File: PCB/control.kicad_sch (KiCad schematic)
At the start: 0 parts

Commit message: Cleaned up the schematic and got started on assigning all the footprints to the symbols
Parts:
- added C20, C21: 0.1 µF, Capacitor_THT:C_Radial_D5.0mm_H5.0mm_P2.00mm, symbol Device:C
- added D38, D39, D40, D41, D42, D43, D44, D45, D46, D47, D48, D49, D50, D51, D52, D53: BLUE, LED_THT:LED_D1.8mm_W1.8mm_H2.4mm_Horizontal_O1.27mm_Z1.6mm, symbol Device:LED
- added D54, D55, D56, D57, D58: GREEN, LED_THT:LED_D1.8mm_W1.8mm_H2.4mm_Horizontal_O1.27mm_Z1.6mm, symbol Device:LED
- added D59, D60, D61: RED, LED_THT:LED_D1.8mm_W1.8mm_H2.4mm_Horizontal_O1.27mm_Z1.6mm, symbol Device:LED
- added R40, R41, R42, R43, R44, R45, R46, R47, R48, R49, R50, R51, R52, R53, R54, R55, R56, R57, R58, R59, R60, R61, R62, R63: 220, Resistor_THT:R_Axial_DIN0207_L6.3mm_D2.5mm_P7.62mm_Horizontal, symbol Device:R
- added R64: 1k, Resistor_THT:R_Axial_DIN0207_L6.3mm_D2.5mm_P7.62mm_Horizontal, symbol Device:R
- added SW8: SW_Push, Button_Switch_THT:SW_PUSH_6mm, symbol Switch:SW_Push
- added U26, U45: 74LS00, symbol 74xx:74LS00
- added U27, U28, U46, U47: 74LS04, symbol 74xx:74LS04
- added U41: 74LS161, symbol 74xx:74LS161
- added U42: 74LS138, symbol 74xx:74LS138
- added U43, U44: AT28C64B-15PU, AT28C64B_15PU:DIP1555W45P254L3733H482Q28, symbol AT28C64B-15PU:AT28C64B-15PU
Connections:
- new net: D44.2 (A), U28.11, U43.12 (I/O1)
- new net: D54.1 (K), U42.11 (O4)
- new net: D54.2 (A), R60.1
- new net: D57.1 (K), U42.14 (O1)
- new net: D57.2 (A), R57.1
- new net: D51.1 (K), R53.1
- new net: D51.2 (A), U44.13 (I/O2), U46.13
- new net: D49.1 (K), R51.1
- new net: R64.1, SW8.1, U26.10, U26.9
- new net: D41.1 (K), R43.1
- new net: D58.2 (A), R56.1
- new net: D59.2 (A), U41.14 (Q0), U42.1 (A0), U43.10 (A0), U44.10 (A0)
- new net: D53.2 (A), U44.11 (I/O0), U46.5
- new net: D52.2 (A), U44.12 (I/O1), U46.11
- new net: D48.2 (A), U44.17 (I/O5), U47.3
- new net: D46.2 (A), U44.19 (I/O7), U47.1
- new net: D61.2 (A), U41.12 (Q2), U42.3 (A2), U43.8 (A2), U44.8 (A2)
- new net: D60.2 (A), U41.13 (Q1), U42.2 (A1), U43.9 (A1), U44.9 (A1)
- new net: D45.2 (A), U28.9, U43.11 (I/O0)
- new net: D52.1 (K), R54.1
- new net: D61.1 (K), R63.1
- new net: D60.1 (K), R62.1
- new net: U26.5, U42.10 (O5)
- new net: U26.6, U45.1, U45.2
- new net: D40.1 (K), R42.1
- new net: D55.1 (K), U42.12 (O3)
- new net: D55.2 (A), R59.1
- new net: D58.1 (K), U42.15 (O0)
- new net: D56.1 (K), U42.13 (O2)
- new net: D56.2 (A), R58.1
- new net: D43.2 (A), U28.13, U43.13 (I/O2)
- new net: D42.2 (A), U28.5, U43.15 (I/O3)
- new net: D41.2 (A), U43.16 (I/O4), U46.3
- new net: D39.2 (A), U43.18 (I/O6), U46.1
- new net: D39.1 (K), R41.1
- new net: D47.1 (K), R49.1
- new net: U41.1 (~{MR}), U45.3
- new net: D53.1 (K), R55.1
- new net: D48.1 (K), R50.1
- new net: D42.1 (K), R44.1
- new net: D45.1 (K), R47.1
- new net: D59.1 (K), R61.1
- new net: D43.1 (K), R45.1
- new net: D46.1 (K), R48.1
- new net: D44.1 (K), R46.1
- new net: D50.1 (K), R52.1
- new net: D38.1 (K), R40.1
- new net CE: D50.2 (A), U44.15 (I/O3)
- new net CF: U43.25 (A8), U44.25 (A8)
- new net CLR: U26.11
- new net GND: C20.2, C21.2, R61.2, R62.2, R63.2, R64.2, U27.7 (GND), U42.4 (E1), U42.5 (E2), U43.14 (GND), U43.2 (A12), U43.20 (~{CE}), U43.21 (A10), U43.22 (~{OE}), U43.23 (A11), U43.3 (A7), U44.14 (GND), U44.2 (A12), U44.20 (~{CE}), U44.21 (A10), U44.22 (~{OE}), U44.23 (A11), U45.7 (GND), U46.7 (GND)
- new net HLT: D38.2 (A), U43.19 (I/O7)
- new net IR_4: U43.7 (A3), U44.7 (A3)
- new net IR_5: U43.6 (A4), U44.6 (A4)
- new net IR_6: U43.5 (A5), U44.5 (A5)
- new net IR_7: U43.4 (A6), U44.4 (A6)
- new net OI: D49.2 (A), U44.16 (I/O4)
- new net RI: D40.2 (A), U43.17 (I/O5)
- new net SU: D47.2 (A), U44.18 (I/O6)
- new net VCC: C20.1, C21.1, R56.2, R57.2, R58.2, R59.2, R60.2, SW8.2, U27.14 (VCC), U41.10 (CET), U41.7 (CEP), U41.9 (~{PE}), U42.6 (E3), U43.27 (~{WE}), U43.28 (VCC), U44.27 (~{WE}), U44.28 (VCC), U44.3 (A7), U45.14 (VCC), U46.14 (VCC)
- new net ZF: U43.24 (A9), U44.24 (A9)
- new net ~{AI}: U28.10
- new net ~{AO}: U28.8
- new net ~{BI}: U47.4
- new net ~{CLK}: U41.2 (CP)
- new net ~{CLR}: U26.12, U26.13, U26.4, U26.8
- new net ~{CO}: U46.12
- new net ~{EO}: U47.2
- new net ~{FI}: U46.6
- new net ~{II}: U28.12
- new net ~{IO}: U28.6
- new net ~{J}: U46.10
- new net ~{MI}: U46.2
- new net ~{RO}: U46.4
- no-connect marks 0 -> 10

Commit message: added more models to work with on my pcb
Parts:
- D38, D39, D40, D41, D42, D43, D44, D45, D46, D47, D48, D49, D50, D51, D52, D53, D54, D55, D56, D57, D58, D59, D60, D61: footprint LED_THT:LED_D1.8mm_W1.8mm_H2.4mm_Horizontal_O1.27mm_Z1.6mm -> LED_THT:LED_D3.0mm
- U26, U27, U28, U45, U46, U47: footprint (none) -> Custom:N14
- U41, U42: footprint (none) -> Custom:N16
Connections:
- net GND: now also R40.2, R41.2, R42.2, R43.2, R44.2, R45.2, R46.2, R47.2, R48.2, R49.2, R50.2, R51.2, R52.2, R53.2, R54.2, R55.2

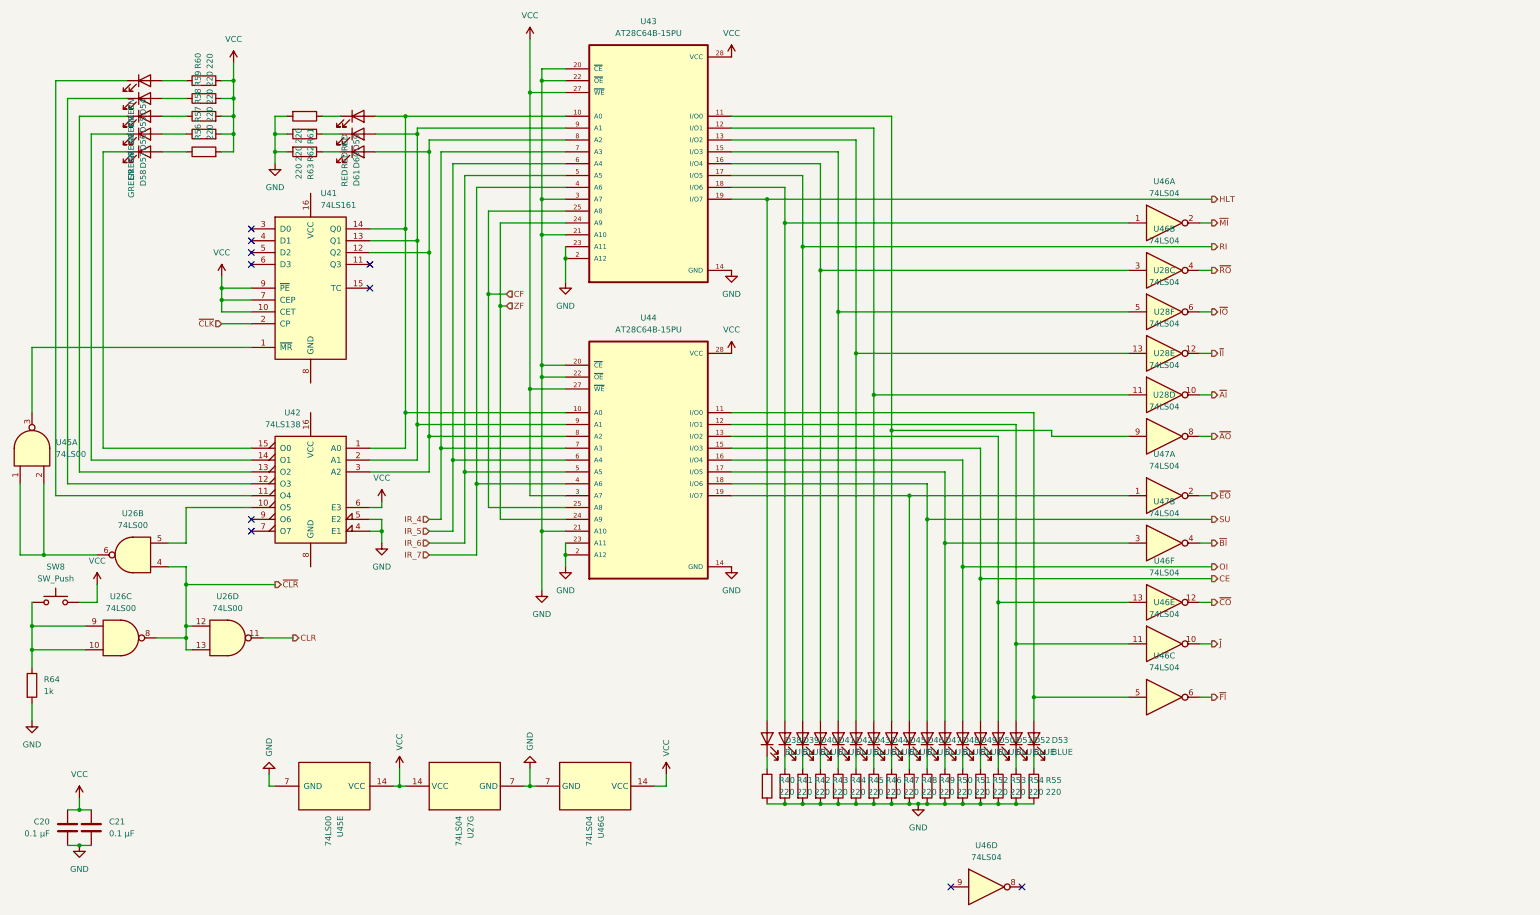
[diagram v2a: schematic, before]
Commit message: Fixed a bunch of ERC errors so know there is only one remaining.
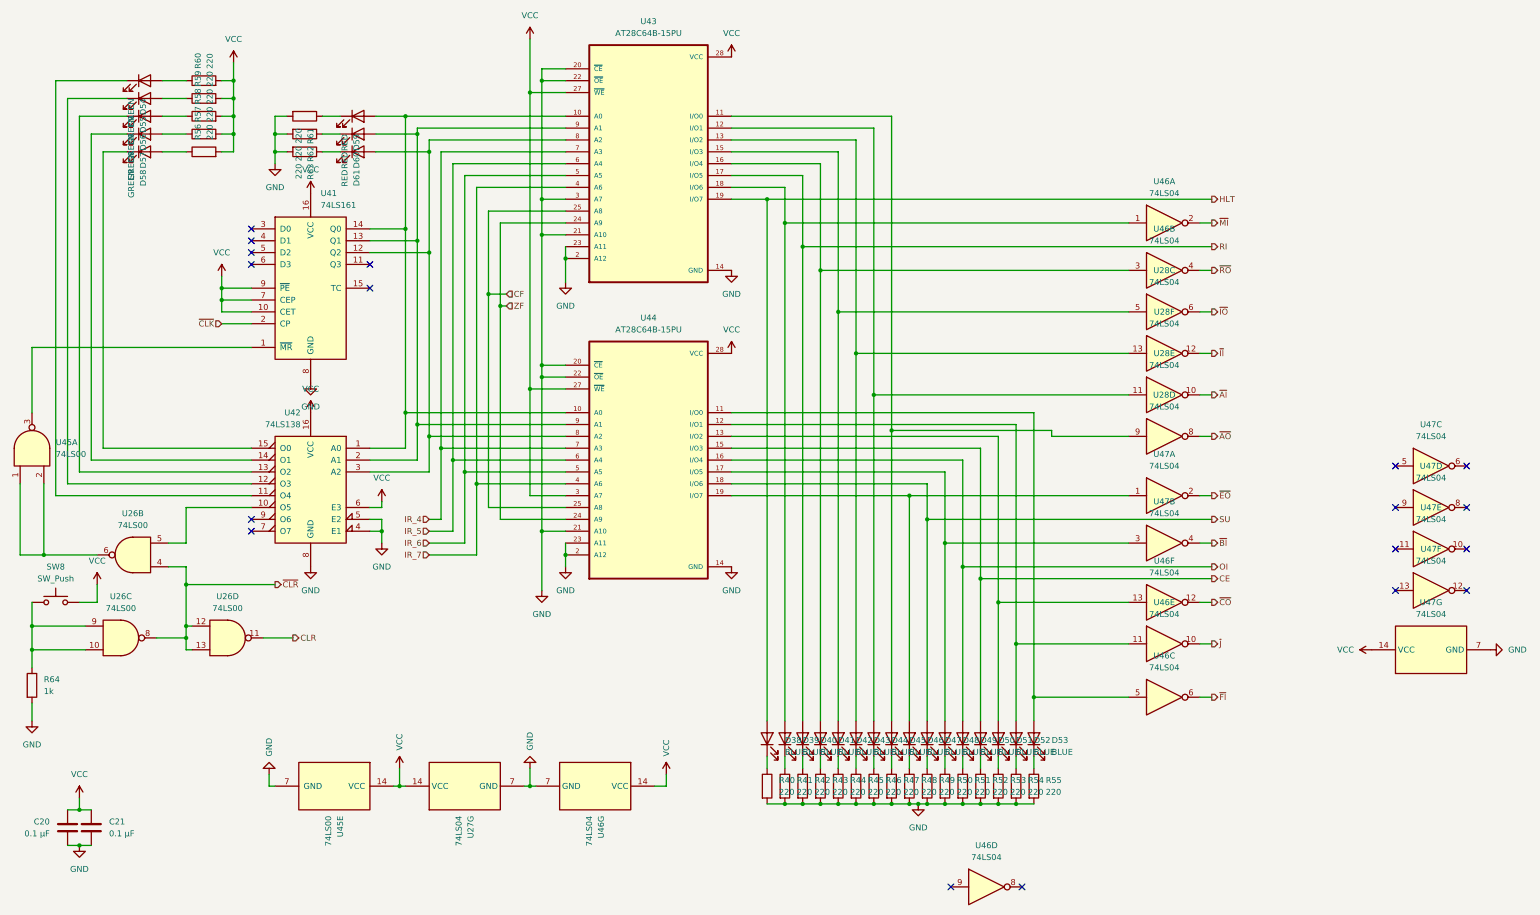
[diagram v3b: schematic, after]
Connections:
- net GND: now also U41.8 (GND), U42.8 (GND), U47.7 (GND)
- net VCC: now also U41.16 (VCC), U42.16 (VCC), U47.14 (VCC)
- no-connect marks 10 -> 18
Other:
- moved on the sheet: U47D

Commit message: Routed the traces for the ground
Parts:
- added unit 3 of U47
- added unit 5 of U47
- added unit 7 of U47
- added unit 6 of U47
- added unit 2 of U47
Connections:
- net GND: now also U47.7 (GND); no longer U47.7 (GND)
- net VCC: now also U47.14 (VCC); no longer U47.14 (VCC)
- net ~{BI}: now also U47.4; no longer U47.4
- net at D48.2 (A), U44.17 (I/O5): now also U47.3; no longer U47.3
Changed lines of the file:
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@@
+	(symbol
+		(lib_id "74xx:74LS04")
+		(at 317.5 147.32 90)
+		(unit 7)
+		(exclude_from_sim no)
+		(in_bom yes)
+		(on_board yes)
+		(dnp no)
+		(fields_autoplaced yes)
+		(property "Reference" "U47"
+			(at 317.5 137.16 90)
+			(effects
+				(font
+					(size 1.27 1.27)
+				)
+			)
+		)
+		(property "Value" "74LS04"
+			(at 317.5 139.7 90)
+			(effects
+				(font
+					(size 1.27 1.27)
+				)
+			)
+		)
+		(property "Footprint" "Custom:N14"
+			(at 317.5 147.32 0)
+			(effects
+				(font
+					(size 1.27 1.27)
+				)
+				(hide yes)
+			)
+		)
+		(property "Datasheet" "http://www.ti.com/lit/gpn/sn74LS04"
+			(at 317.5 147.32 0)
+			(effects
+				(font
+					(size 1.27 1.27)
+				)
+				(hide yes)
+			)
+		)
+		(property "Description" "Hex Inverter"
+			(at 317.5 147.32 0)
+			(effects
+				(font
+					(size 1.27 1.27)
+				)
+				(hide yes)
+			)
+		)
+		(pin "3"
+		)
+		(pin "2"
+		)
+		(pin "1"
+		)
+		(pin "4"
+		)
+		(pin "9"
+		)
+		(pin "6"
+		)
+		(pin "5"
+		)
+		(pin "14"
+		)
+		(pin "12"
+		)
+		(pin "8"
+		)
+		(pin "11"
+		)
+		(pin "13"
+		)
+		(pin "10"
+		)
+		(pin "7"
+		)
+		(instances
+			(project ""
+				(path "/48633dea-2de9-4b6f-aeff-2ee54233f918/d073e50d-b064-481f-8def-abf1072e09eb"
+					(reference "U47")
+					(unit 7)
+				)
+			)
+		)
+	)
 	(symbol
 		(lib_id "74xx:74LS04")
@@
 				)
 			)
-		)
-	)
-	(symbol
-		(lib_id "74xx:74LS04")
-		(at 317.5 147.32 90)
-		(unit 7)
-		(exclude_from_sim no)
-		(in_bom yes)
-		(on_board yes)
-		(dnp no)
-		(fields_autoplaced yes)
-		(property "Reference" "U47"
-			(at 317.5 137.16 90)
-			(effects
-				(font
-					(size 1.27 1.27)
-				)
-			)
-		)
-		(property "Value" "74LS04"
-			(at 317.5 139.7 90)
-			(effects
-				(font
-					(size 1.27 1.27)
-				)
-			)
-		)
-		(property "Footprint" "Custom:N14"
-			(at 317.5 147.32 0)
-			(effects
-				(font
-					(size 1.27 1.27)
-				)
-				(hide yes)
-			)
-		)
-		(property "Datasheet" "http://www.ti.com/lit/gpn/sn74LS04"
-			(at 317.5 147.32 0)
-			(effects
-				(font
-					(size 1.27 1.27)
-				)
-				(hide yes)
-			)
-		)
-		(property "Description" "Hex Inverter"
-			(at 317.5 147.32 0)
-			(effects
-				(font
-					(size 1.27 1.27)
-				)
-				(hide yes)
-			)
-		)
-		(pin "3"
-		)
-		(pin "2"
-		)
-		(pin "1"
-		)
-		(pin "4"
-		)
-		(pin "9"
-		)
-		(pin "6"
-		)
-		(pin "5"
-		)
-		(pin "14"
-		)
-		(pin "12"
-		)
-		(pin "8"
-		)
-		(pin "11"
-		)
-		(pin "13"
-		)
-		(pin "10"
-		)
-		(pin "7"
-		)
-		(instances
-			(project ""
-				(path "/48633dea-2de9-4b6f-aeff-2ee54233f918/d073e50d-b064-481f-8def-abf1072e09eb"
-					(reference "U47")
-					(unit 7)
-				)
-			)

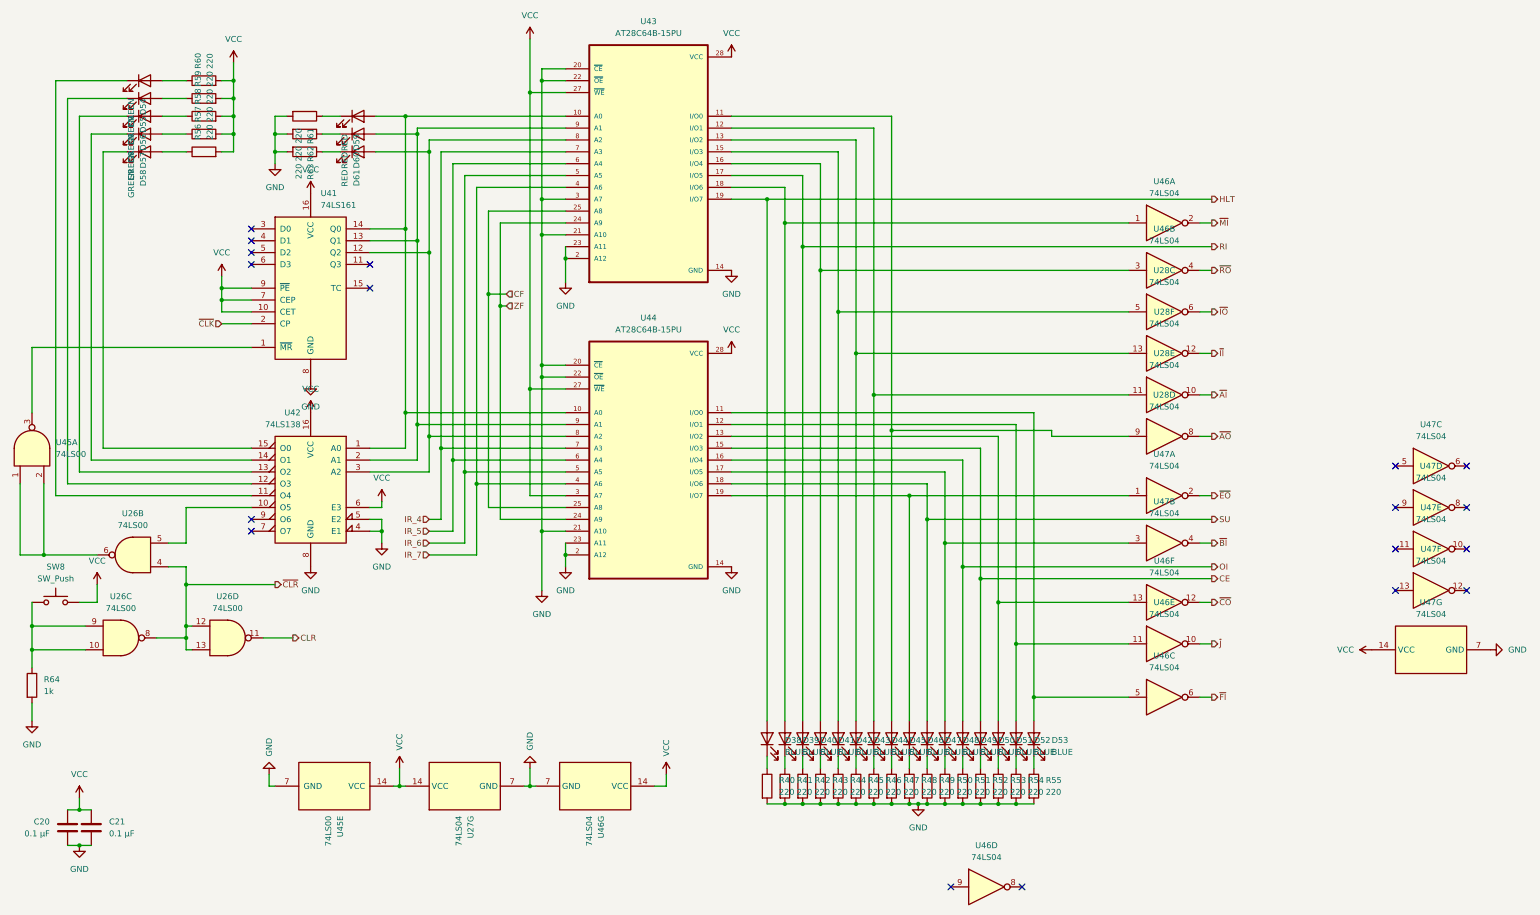
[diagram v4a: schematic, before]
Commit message: Add decupling caps and reroute pcb. Updated BOM to match new number of caps
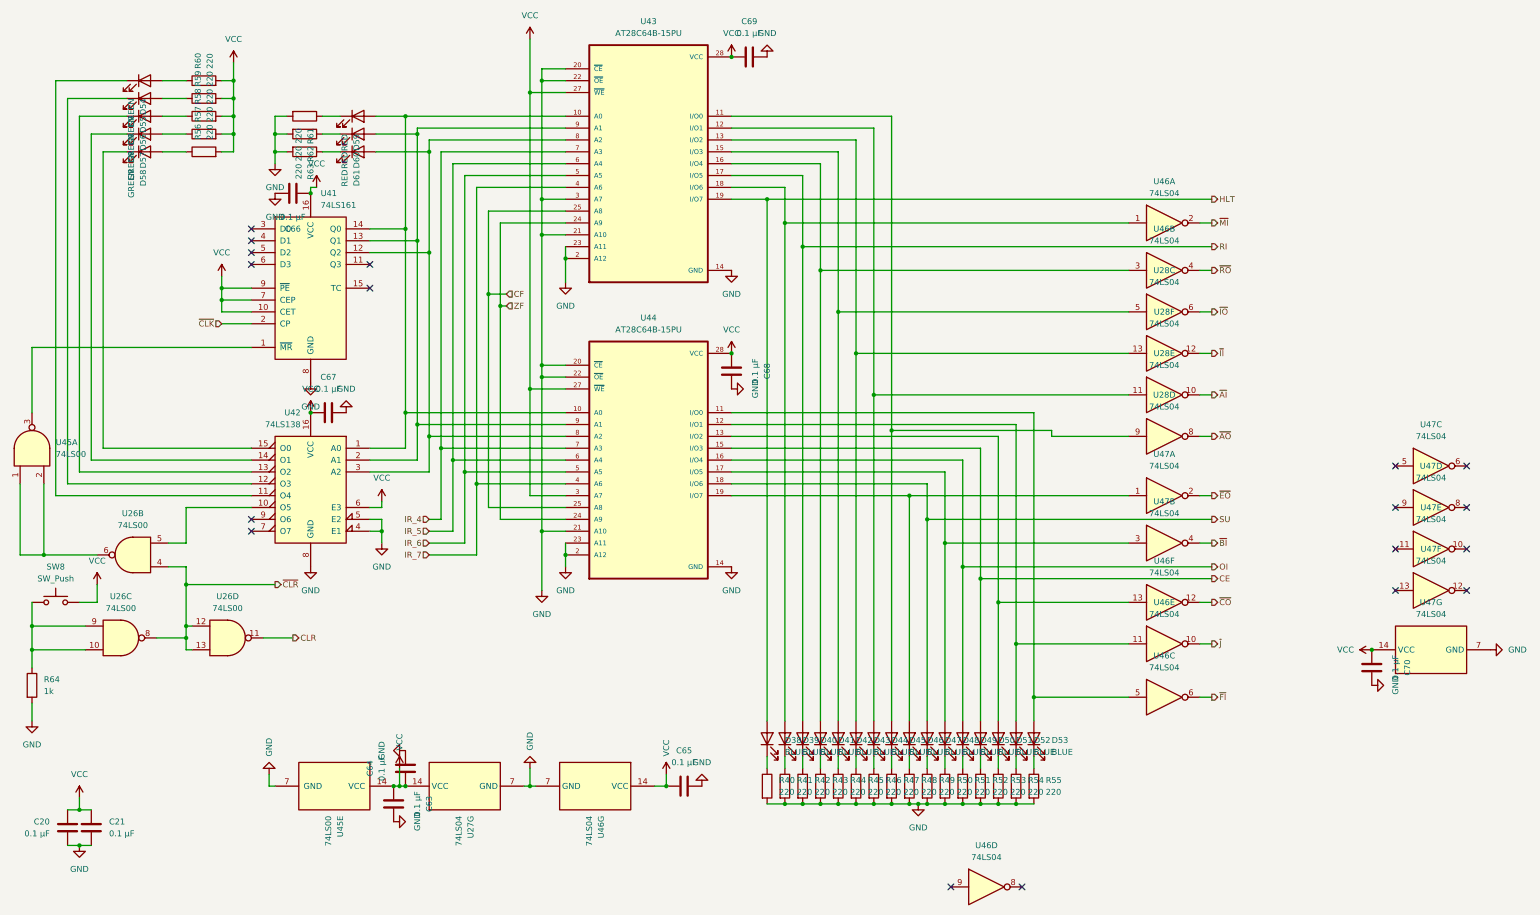
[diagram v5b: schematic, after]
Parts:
- added C63, C64, C65, C66, C67, C68, C69, C70: 0.1 µF, Capacitor_THT:C_Radial_D5.0mm_H5.0mm_P2.00mm, symbol Device:C
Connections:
- net GND: now also C63.2, C64.2, C65.2, C66.2, C67.2, C68.2, C69.2, C70.2
- net VCC: now also C63.1, C64.1, C65.1, C66.1, C67.1, C68.1, C69.1, C70.1

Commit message: Redoing PCB layout and fixed some signal flow convention errors
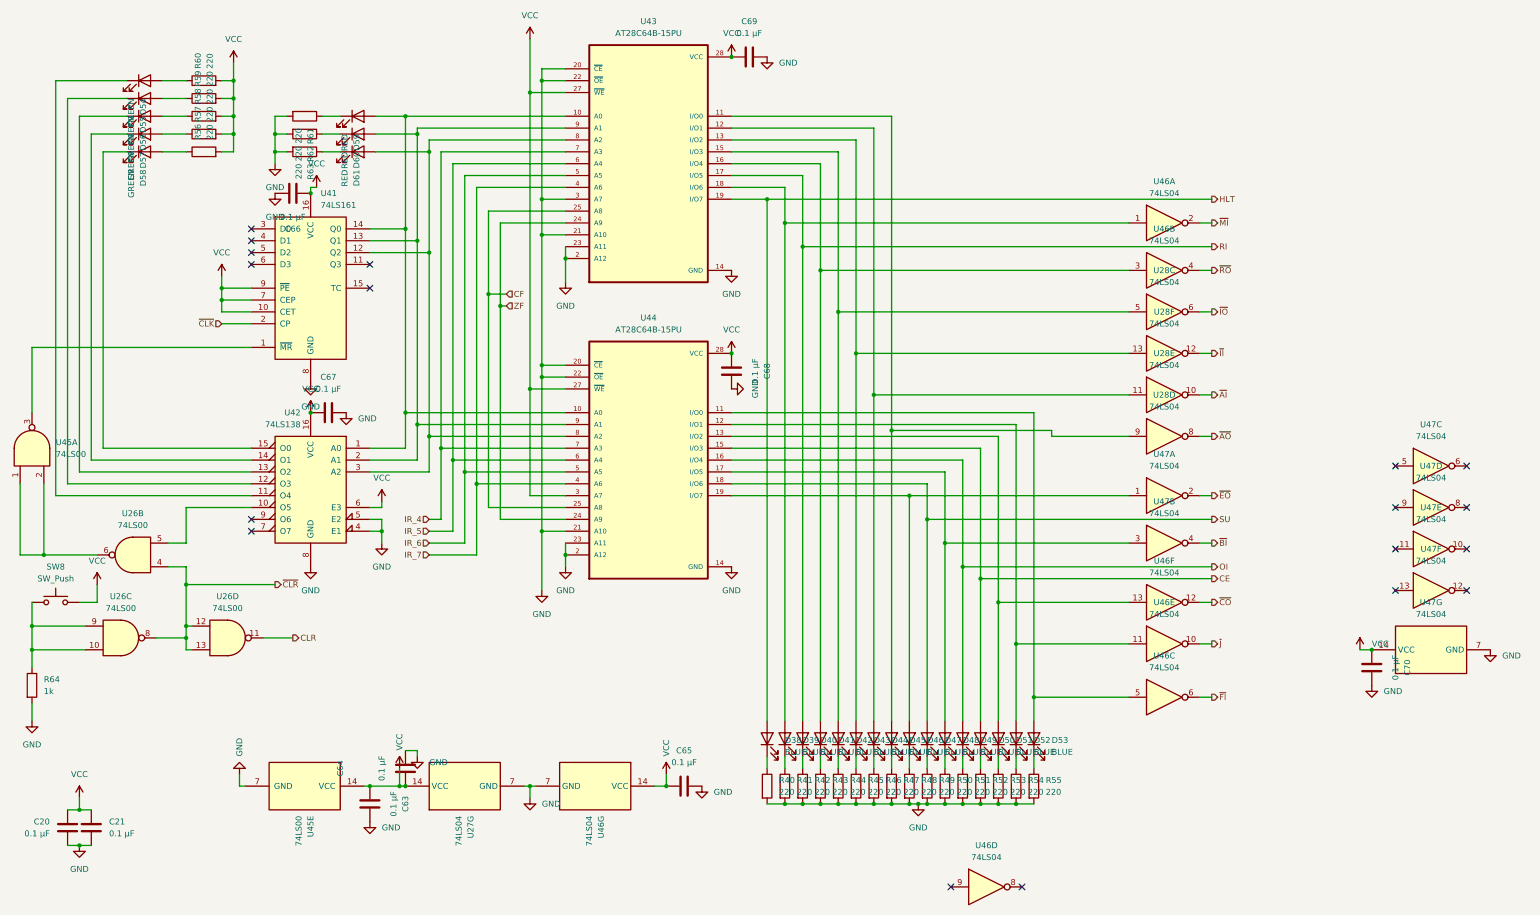
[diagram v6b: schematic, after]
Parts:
- U43, U44: footprint AT28C64B_15PU:DIP1555W45P254L3733H482Q28 -> Package_DIP:DIP-28_W15.24mm
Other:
- moved on the sheet: C63, U45E
